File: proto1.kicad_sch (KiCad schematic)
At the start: 27 parts, among them J11 TC2030, J12 PA_L, J14 PA_L, J15 PA_L, J16 PA_L, J17 PA_L, J18 PA_L, J2 Conn_01x05, J3 LCD, SW1 RESET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

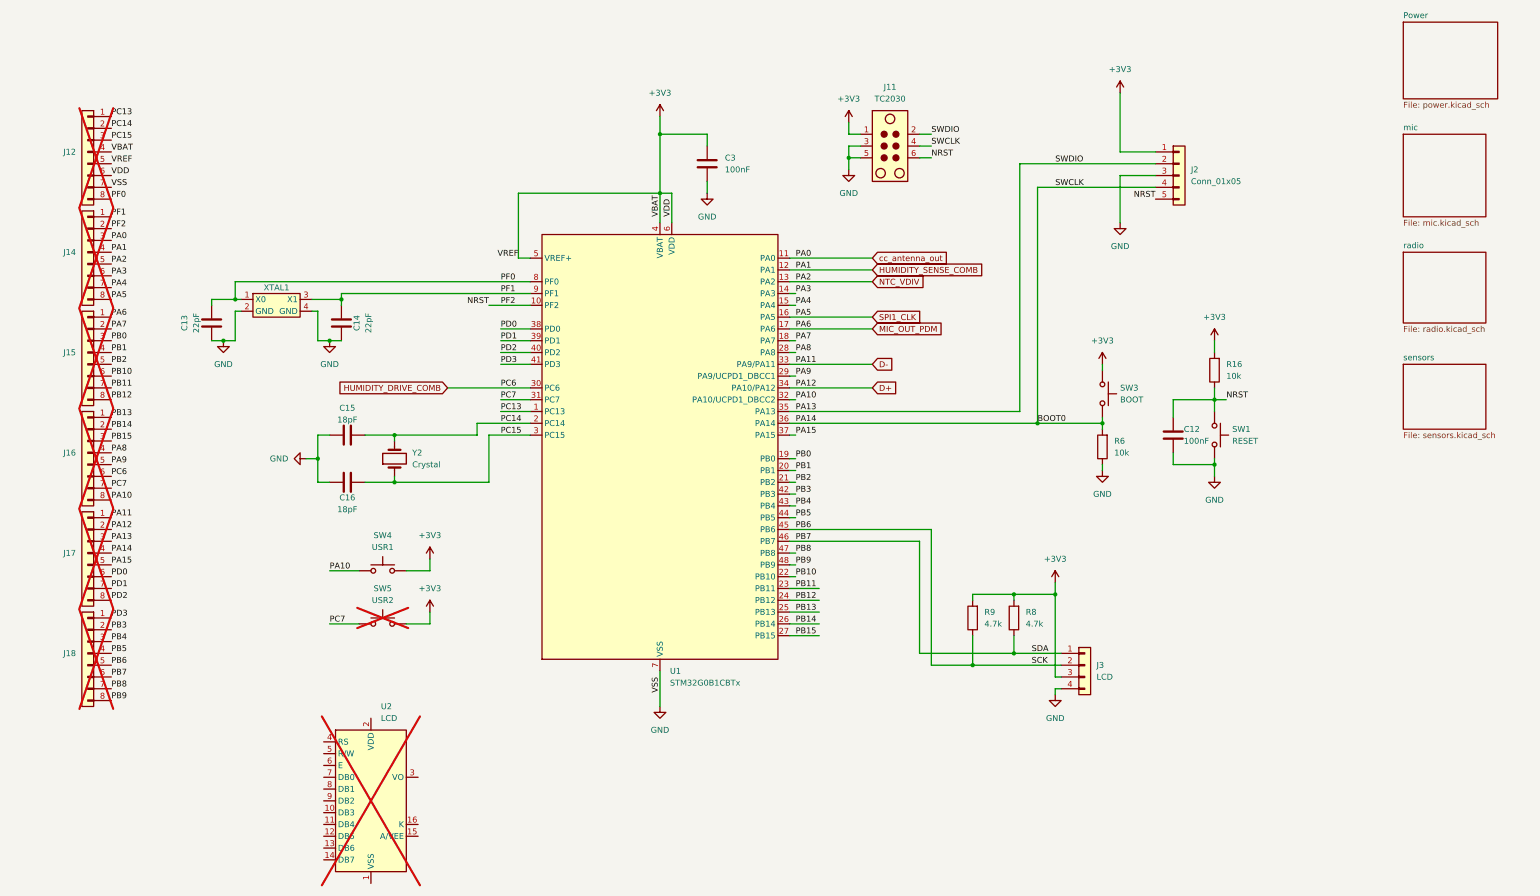
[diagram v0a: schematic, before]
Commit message: refactor hierarchical sheets to use sheet pins
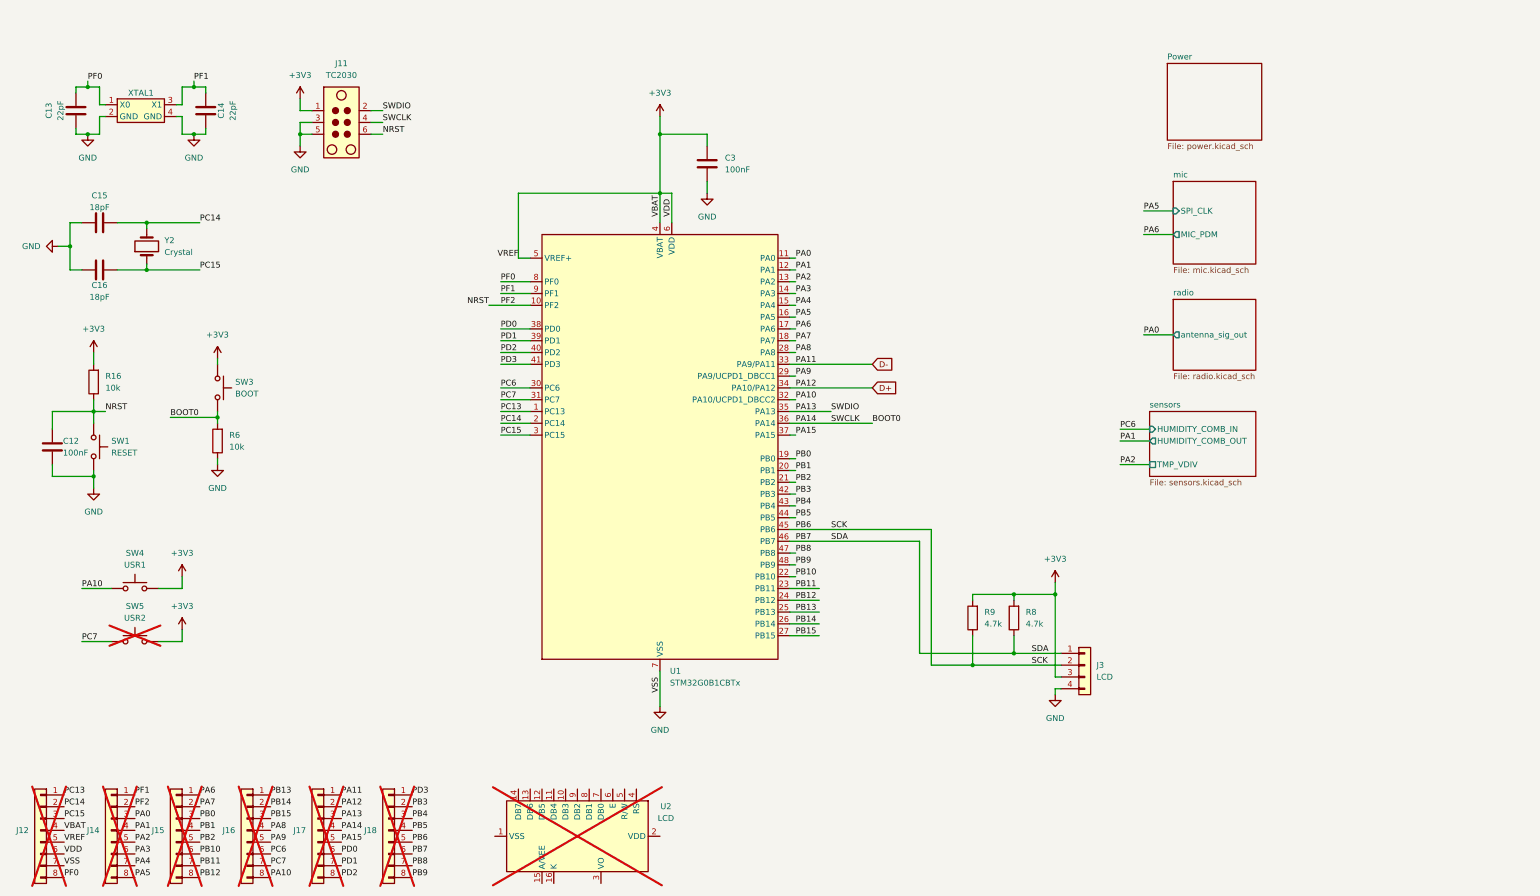
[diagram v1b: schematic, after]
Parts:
- removed J2: Conn_01x05, symbol Connector_Generic:Conn_01x05
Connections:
- net HUMIDITY_DRIVE_COMB renamed PC6
- net HUMIDITY_SENSE_COMB renamed PA1
- net MIC_OUT_PDM renamed PA6
- net NTC_VDIV renamed PA2
- net SPI1_CLK renamed PA5
- net cc_antenna_out renamed PA0
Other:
- sheet mic ports: added MIC_PDM, SPI_CLK; removed none
- sheet radio ports: added antenna_sig_out; removed none
- sheet sensors ports: added HUMIDITY_COMB_IN, HUMIDITY_COMB_OUT, TMP_VDIV; removed none
- moved on the sheet: C12, C13, C14, C15, C16, J11, J12, J14, J15, J16, J17, J18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

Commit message: WIP relayout of board
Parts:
- C12: footprint Capacitor_SMD:C_0603_1608Metric -> Capacitor_SMD:C_0402_1005Metric
- C3: footprint Capacitor_SMD:C_0402_1005Metric_Pad0.74x0.62mm_HandSolder -> Capacitor_SMD:C_0402_1005Metric
- R16, R6, R8, R9: footprint Resistor_SMD:R_0603_1608Metric -> Resistor_SMD:R_0402_1005Metric
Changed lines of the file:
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@@
 		)
 	)
+	(label "PB15"
+		(at 251.46 96.52 0)
+		(effects
+			(font
+				(size 1.27 1.27)
+			)
+			(justify left bottom)
+		)
+	)
 	(label "PA2"
 		(at 39.37 185.42 0)
@@
 		)
 	)
-	(label "PC6"
-		(at 251.46 96.52 0)
-		(effects
-			(font
-				(size 1.27 1.27)
-			)
-			(justify left bottom)
-		)
-	)
 	(label "PA5"
 		(at 256.54 49.53 0)
@@
 			)
 		)
-		(property "Footprint" "Resistor_SMD:R_0603_1608Metric"
+		(property "Footprint" "Resistor_SMD:R_0402_1005Metric"
 			(at 58.928 99.06 90)
 			(effects
@@
 			)
 		)
-		(property "Footprint" "Resistor_SMD:R_0603_1608Metric"
+		(property "Footprint" "Resistor_SMD:R_0402_1005Metric"
 			(at 221.488 137.16 90)
 			(effects
@@
 			)
 		)
-		(property "Footprint" "Capacitor_SMD:C_0603_1608Metric"
+		(property "Footprint" "Capacitor_SMD:C_0402_1005Metric"
 			(at 22.5552 104.14 0)
 			(effects
@@
 			)
 		)
-		(property "Footprint" "Resistor_SMD:R_0603_1608Metric"
+		(property "Footprint" "Resistor_SMD:R_0402_1005Metric"
 			(at 32.258 86.36 90)
 			(effects
@@
 			)
 		)
-		(property "Footprint" "Capacitor_SMD:C_0402_1005Metric_Pad0.74x0.62mm_HandSolder"
+		(property "Footprint" "Capacitor_SMD:C_0402_1005Metric"
 			(at 163.5252 43.18 0)
 			(effects
@@
 			)
 		)
-		(property "Footprint" "Resistor_SMD:R_0603_1608Metric"
+		(property "Footprint" "Resistor_SMD:R_0402_1005Metric"
 			(at 230.378 137.16 90)
 			(effects

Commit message: Board V3
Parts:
- added C18, C19: 100nF, Capacitor_SMD:C_0402_1005Metric, symbol Device:C
- added D5: LED Blue, LED_SMD:LED_0603_1608Metric, symbol Device:LED
- added J2: Conn_01x03, Connector_PinHeader_2.54mm:PinHeader_1x03_P2.54mm_Vertical, symbol Connector_Generic:Conn_01x03
- added R19: 100Ω, Resistor_SMD:R_0402_1005Metric, symbol Device:R
- added R4, R5: 10k, Resistor_SMD:R_0402_1005Metric, symbol Device:R
- C12, C3: Est Cost 0.002 -> (none); Est Cost (1000) (none) -> 0.0007; LCSC (none) -> https://www.lcsc.com/product-detail/C22435938.html; Manufacturer (none) -> HRE; Part No (none) -> CGA0402X7R104K6R3GT; Type (none) -> SMD; Vendor https://www.lcsc.com/product-detail/C6119883.html -> (none)
- C13, C14: Est Cost 0.0007 -> (none); Est Cost (1000) (none) -> 0.0007; LCSC (none) -> https://www.lcsc.com/product-detail/C42371856.html; Manufacturer (none) -> HRE; Part No (none) -> CGA0402C0G220J500GT; Type (none) -> SMD; Vendor https://www.lcsc.com/product-detail/C42371856.html -> (none)
- C15, C16: value 18pF -> 15pF; footprint Capacitor_SMD:C_0402_1005Metric_Pad0.74x0.62mm_HandSolder -> Capacitor_SMD:C_0402_1005Metric; Est Cost 0.0006 -> (none); Est Cost (1000) (none) -> 0.0006; LCSC (none) -> https://www.lcsc.com/product-detail/C45359895.html; Manufacturer (none) -> HRE; Part No (none) -> CGA0402C0G150J500GT; Type (none) -> SMD; Vendor https://www.lcsc.com/product-detail/C45359896.html -> (none)
- J12, J14, J15, J16, J17, J18: Est Cost (1000) (none) -> 0.1009; Height (none) -> 9mm; LCSC (none) -> https://www.lcsc.com/product-detail/C41397108.html; Manufacturer (none) -> hanxia; Part No (none) -> HX PM1.27-1x8P TP-YQ; Vendor https://www.lcsc.com/product-detail/C41397108.html -> (none)
- J3: Est Cost 0.0636 -> (none); Est Cost (1000) (none) -> 0.0636; Height (none) -> 9mm; LCSC (none) -> https://www.lcsc.com/product-detail/C20071191.html; Manufacturer (none) -> Yxcon; Part No (none) -> F136-1104S3CMUB2; Type (none) -> SMD; Vendor https://www.lcsc.com/product-detail/C20071191.html -> (none)
- R16, R6: Est Cost 0.0006 -> (none); Est Cost (1000) (none) -> 0.0003; LCSC (none) -> https://www.lcsc.com/product-detail/C3017497.html; Manufacturer (none) -> VO; Part No (none) -> SCR0402J10K; Type (none) -> SMD; Vendor https://www.lcsc.com/product-detail/C2930027.html -> (none)
- R8, R9: Est Cost 0.0006 -> (none); Est Cost (1000) (none) -> 0.0004; LCSC (none) -> https://www.lcsc.com/product-detail/C2906941.html; Manufacturer (none) -> FOJAN; Part No (none) -> FRC0402J472 TS; Type (none) -> SMD; Vendor https://www.lcsc.com/product-detail/C49254210.html -> (none)
- SW1, SW3, SW4: Est Cost 0.0074 -> (none); Est Cost (1000) (none) -> 0.0055; Height (none) -> 4.5mm; LCSC (none) -> https://www.lcsc.com/product-detail/C22375351.html; Manufacturer (none) -> HanElectricity; Part No (none) -> TS110926045; Type (none) -> SMD; Vendor https://www.lcsc.com/product-detail/C22375351.html -> (none)
- SW5: Est Cost 0.0074 -> (none); Est Cost (1000) (none) -> 0.0055; Height (none) -> 4.5mm; LCSC (none) -> https://www.lcsc.com/product-detail/C22375351.html; Manufacturer (none) -> HanElectricity; Part No (none) -> TS110926045; Type (none) -> SMD; Vendor https://www.lcsc.com/product-detail/C22375351.html -> (none); now fitted; now in the parts list
- U1: Est Cost 1.17 -> (none); Est Cost (1000) (none) -> 1.22; Height (none) -> 1.6mm; LCSC (none) -> https://www.lcsc.com/product-detail/C2847904.html; Manufacturer (none) -> ST; Part No (none) -> STM32G0B1CBT6; Type (none) -> SMD; Vendor https://www.lcsc.com/product-detail/C2847904.html -> (none)
- U2: footprint (none) -> Display:RC1602A; Alibaba (none) -> https://www.alibaba.com/product-detail/Stock-0-91-Inch-128x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; Est Cost AUD 1.48 -> 1.68; Type (none) -> Module; Vendor https://www.alibaba.com/product-detail/Stock-0-91-Inch-128x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 -> (none)
- XTAL1: value ~ -> 8Mz CL=20pF; Est Cost 0.0674 -> (none); Est Cost (1000) (none) -> 0.0684; Height (none) -> 0.7mm; LCSC (none) -> https://www.lcsc.com/product-detail/C19723454.html; Manufacturer (none) -> Yajingxin; Part No (none) -> TX32258M4LBDE2T; Type (none) -> SMD; Vendor https://www.lcsc.com/product-detail/C5310727.html -> (none)
- Y2: value Crystal -> 32.768KHz 12.5pF 70kΩ; footprint Crystal:Crystal_SMD_0603-2Pin_6.0x3.5mm -> Crystal:Crystal_SMD_EuroQuartz_EQ161-2Pin_3.2x1.5mm; Est Cost 0.059 -> (none); Est Cost (1000) (none) -> 0.0784; Height (none) -> 0.8mm; LCSC (none) -> https://www.lcsc.com/product-detail/C19723454.html; Manufacturer (none) -> huaxindianzi; Part No (none) -> 3K32.768XQ; Type (none) -> SMD; Vendor https://www.lcsc.com/product-detail/C51822844.html -> (none)
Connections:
- net BOOT0: now also J2.2 (Pin_2)
- net GND: now also C18.2, C19.2, D5.1 (K), R4.1, R5.1
- net NRST: now also J2.3 (Pin_3)
- net PA10: now also C18.1, R4.2
- net PA13: now also J2.1 (Pin_1)
- net PC6: now also R19.1
- net PC7: now also C19.1, R5.2
- net PC14 renamed LSE_P
- net PC15 renamed LSE_N
- new net: D5.2 (A), R19.2
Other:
- sheet sensors ports: added LIGHT_VDIV; removed none
- moved on the sheet: J3, R8, R9, SW4
